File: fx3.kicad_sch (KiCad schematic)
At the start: 64 parts, among them J4 JTAG, J5 UART, SW1 RESET, U2 CYUSB3014-BZXI, U3 24LC1025-I/SN, Y1 19.2MHz

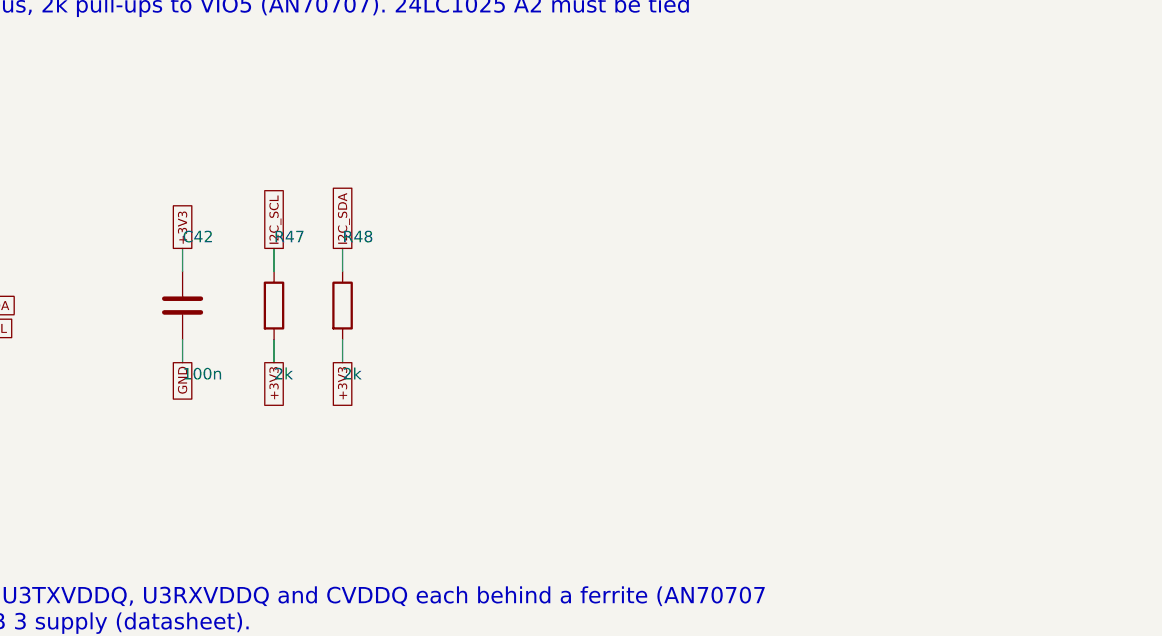
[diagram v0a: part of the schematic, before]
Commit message: Footprints: TVP7002 pad and vias per the OSSC, FX3 pads per AN70707; spare boot EEPROM
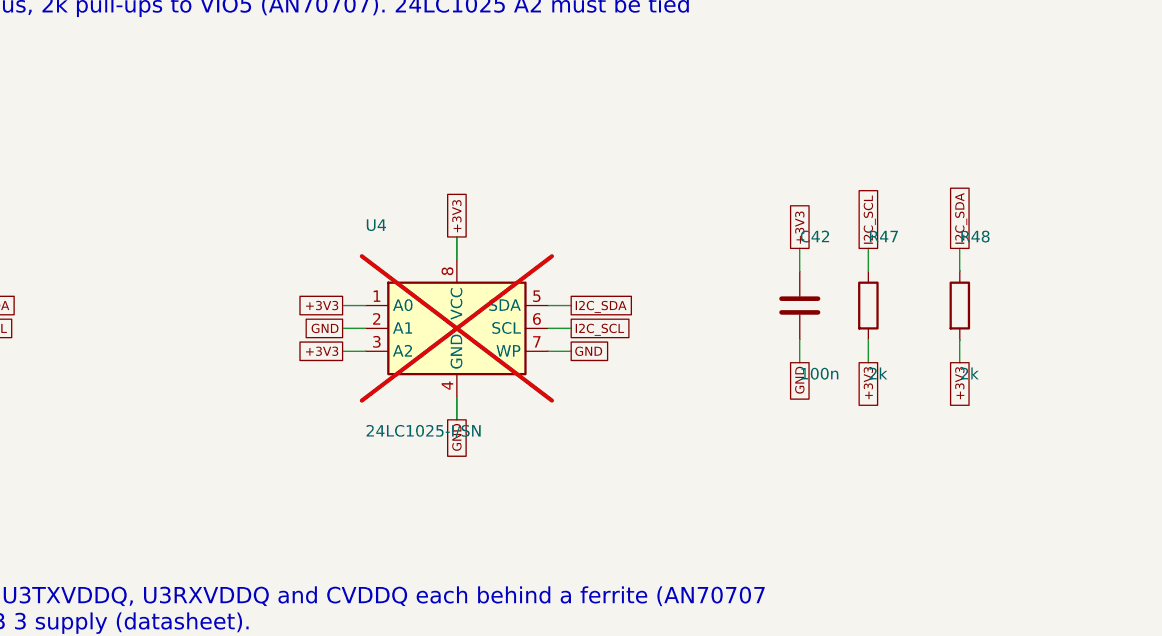
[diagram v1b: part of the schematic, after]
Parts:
- added U4: 24LC1025-I/SN, Package_SO:SOIC-8_3.9x4.9mm_P1.27mm, symbol Memory_EEPROM:24LC1025
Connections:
- net +3V3: now also U4.1 (A0), U4.3 (A2), U4.8 (VCC)
- net GND: now also U4.2 (A1), U4.4 (GND), U4.7 (WP)
- net I2C_SCL: now also U4.6 (SCL)
- net I2C_SDA: now also U4.5 (SDA)

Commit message: Status LED: common-anode RGB on FX3 GPIO50-52, firmware state map
XL-1615RGBC-RF (C965840) replaces the GPIO57 debug LED. Its LCSC pattern
numbers G and B the other way from the datasheet; fix_footprints.py renumbers
them and applies the datasheet's land pattern. GPIO budget in docs/design.md.
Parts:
- removed D3: GREEN, LED_SMD:LED_0603_1608Metric, symbol Device:LED
- added D3: XL-1615RGBC-RF, ps1-av-capture:LED-ARRAY-SMD_4P-L1.6-W1.5-BR_XL-1615RGBC-RF, symbol Device:LED_RAGB
- added R52, R53: 100, Resistor_SMD:R_0402_1005Metric, symbol Device:R
- R51: value 1k -> 470; LCSC C11702 -> C25117
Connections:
- net +3V3: now also D3.2 (A)
- net LED_R: now reaches U2.D1 (GPIO[50])
- net LED_R: now also R51.2
- net LED_G: now reaches U2.D2 (GPIO[51])
- net LED_G: now also R52.2
- net LED_B: now reaches U2.D3 (GPIO[52])
- net LED_B: now also R53.2
- net FX3_LED: no longer names the net of U2.C4 (GPIO[57])
- net FX3_LED: no longer R51.2
- net FX3_LED_K renamed LED_R_K
- net LED_R_K: now also D3.1 (RK)
- new net LED_B_K: D3.4 (BK), R53.1
- new net LED_G_K: D3.3 (GK), R52.1
- no-connect marks 30 -> 28
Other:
- note added: "Debug: JTAG (no external pulls; FX3 has internal ones), UART on GPIO55/56."
- note added: "Status LED: common-anode RGB on +3V3, cathodes sunk by GPIO50/51/52 (the unused I2S balls). Pin order per the XL-1615RGBC-RF datasheet: 1 R, 2 common anode, 3 G, 4 B. States in docs/design.md."
- note removed: "Debug: JTAG (no external pulls; FX3 has internal ones), UART on GPIO55/56, LED on GPIO57."
